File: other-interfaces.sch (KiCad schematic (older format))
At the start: 14 parts, among them J9 693072010801

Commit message: Change uSD card holder
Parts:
- removed J9: 693072010801, sa800u-baseboard-hw-footprints:MicroSD_693072010801, symbol sa800u-baseboard-hw:693072010801
- added J5: DM3AT-SF-PEJM5, antmicro-footprints:MicroSD_DM3AT-SF-PEJM5, symbol antmicroMemoryConnectorsPCCardSockets:DM3AT-SF-PEJM5
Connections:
- wire segments 51 -> 56
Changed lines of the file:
@@
 Text
 Wire Wire Line
-	2700 2600 2700 2675
-Wire Wire Line
-	2700 2275 2700 2300
-Wire Wire Line
-	2500 2275 2700 2275
-Wire Wire Line
-	2700 2675 2675 2675
-Connection ~ 2700 2675
+	5900 3275 5850 3275
+$Comp
+L sa800u-baseboard-hw:GND #PWR?
+U 1 1 61F78331
+P 5850 3775
+AR Path="/61A60486/61F78331" Ref="#PWR?"  Part="1"
+AR Path="/61C01D88/61F78331" Ref="#PWR0191"  Part="1"
+F 0 "#PWR0191" H 5850 3525 50  0001 C CNN
+F 1 "GND" H 5855 3602 50  0000 C CNN
+F 2 "" H 5850 3775 50  0001 C CNN
+F 3 "" H 5850 3775 50  0001 C CNN
+	1    5850 3775
+	1    0    0    -1
+$EndComp
+$Comp
+L sa800u-baseboard-hw:GND #PWR?
+U 1 1 61F9BA66
+P 7650 3725
+AR Path="/61A60486/61F9BA66" Ref="#PWR?"  Part="1"
+AR Path="/61C01D88/61F9BA66" Ref="#PWR0256"  Part="1"
+F 0 "#PWR0256" H 7650 3475 50  0001 C CNN
+F 1 "GND" H 7655 3552 50  0000 C CNN
+F 2 "" H 7650 3725 50  0001 C CNN
+F 3 "" H 7650 3725 50  0001 C CNN
+	1    7650 3725
+	1    0    0    -1
+$EndComp
+Wire Wire Line
+	7600 3675 7650 3675
+Wire Wire Line
+	7650 3675 7650 3725
+Wire Wire Line
+	5850 3675 5850 3775
+$Comp
+L antmicroMemoryConnectorsPCCardSockets:DM3AT-SF-PEJM5 J5
+U 1 1 62685888
+P 6800 3175
+F 0 "J5" H 6750 4174 50  0000 C CNN
+F 1 "DM3AT-SF-PEJM5" H 6750 4083 50  0000 C CNN
+F 2 "antmicro-footprints:MicroSD_DM3AT-SF-PEJM5" H 6800 3175 50  0001 C CNN
+F 3 "" H 6800 3175 50  0001 C CNN
+F 4 "HIROSE" H 6750 3992 50  0000 C CNN "Manufacturer"
+F 5 "DM3AT-SF-PEJM5" H 6750 3901 50  0000 C CNN "MPN"
+	1    6800 3175
+	1    0    0    -1
+$EndComp
+Wire Wire Line
+	5850 3275 5850 3675
+Wire Wire Line
+	5850 3675 5900 3675
+Connection ~ 5850 3675
 Wire Wire Line
 	2725 3475 2675 3475
@@
 	1    0    0    -1
 $EndComp
-Text GLabel 2675 3075 0    50   Input ~ 0
-SD_LDO21A
 $Comp
 L sa800u-baseboard-hw:R_1k_0402 R105
@@
 	1    0    0    -1
 $EndComp
-Text GLabel 2675 2775 0    50   Input ~ 0
-SD_DATA2
-Text GLabel 2675 2875 0    50   Input ~ 0
-SD_DATA3
-Text GLabel 2675 3475 0    50   Input ~ 0
-SD_DATA1
-Text GLabel 2675 3375 0    50   Input ~ 0
-SD_DATA0
-Text GLabel 2675 2675 0    50   Input ~ 0
-SD_DET
-Text GLabel 2675 2975 0    50   Input ~ 0
-SD_CMD
-Text GLabel 2675 3175 0    50   Input ~ 0
-SD_CLK
 Wire Wire Line
 	4250 3725 4250 2775
@@
 Wire Wire Line
 	5375 3725 5375 3475
-Wire Wire Line
-	5900 3275 5850 3275
-$Comp
-L sa800u-baseboard-hw:GND #PWR?
-U 1 1 61F78331
-P 5850 3625
-AR Path="/61A60486/61F78331" Ref="#PWR?"  Part="1"
-AR Path="/61C01D88/61F78331" Ref="#PWR0191"  Part="1"
-F 0 "#PWR0191" H 5850 3375 50  0001 C CNN
-F 1 "GND" H 5855 3452 50  0000 C CNN
-F 2 "" H 5850 3625 50  0001 C CNN
-F 3 "" H 5850 3625 50  0001 C CNN
-	1    5850 3625
-	1    0    0    -1
-$EndComp
 $Comp
 L sa800u-baseboard-hw:GND #PWR?
@@
 Wire Wire Line
 	5075 3725 5075 3075
-$Comp
-L sa800u-baseboard-hw:C_10p_0402 C124
-U 1 1 62000138
-P 5150 2300
-F 0 "C124" H 5265 2345 60  0000 L CNN
-F 1 "C_10p_0402" H 5150 2150 60  0001 C CNN
-F 2 "sa800u-baseboard-hw-footprints:0402-cap" H 5350 2500 60  0001 L CNN
-F 3 "" H 5150 2300 50  0001 C CNN
-F 4 "MULTICOMP" H 5350 2700 60  0001 L CNN "Manufacturer"
-F 5 "MC0402N100D500CT" H 5350 2600 60  0001 L CNN "MPN"
-F 6 "10p" H 5265 2247 50  0000 L CNN "Val"
-	1    5150 2300
-	1    0    0    -1
-$EndComp
-Wire Wire Line
-	5075 2150 5150 2150
-$Comp
-L sa800u-baseboard-hw:GND #PWR?
-U 1 1 62009F3E
-P 5150 2450
-AR Path="/61A60486/62009F3E" Ref="#PWR?"  Part="1"
-AR Path="/61C01D88/62009F3E" Ref="#PWR0184"  Part="1"
-F 0 "#PWR0184" H 5150 2200 50  0001 C CNN
-F 1 "GND" H 5155 2277 50  0000 C CNN
-F 2 "" H 5150 2450 50  0001 C CNN
-F 3 "" H 5150 2450 50  0001 C CNN
-	1    5150 2450
-	1    0    0    -1
-$EndComp
-$Comp
-L sa800u-baseboard-hw:GND #PWR?
-U 1 1 6200C035
-P 5575 2450
-AR Path="/61A60486/6200C035" Ref="#PWR?"  Part="1"
-AR Path="/61C01D88/6200C035" Ref="#PWR0185"  Part="1"
-F 0 "#PWR0185" H 5575 2200 50  0001 C CNN
-F 1 "GND" H 5580 2277 50  0000 C CNN
-F 2 "" H 5575 2450 50  0001 C CNN
-F 3 "" H 5575 2450 50  0001 C CNN
-	1    5575 2450
-	1    0    0    -1
-$EndComp
-Connection ~ 5150 2150
-Wire Wire Line
-	5150 2150 5575 2150
-$Comp
-L sa800u-baseboard-hw:C_2u2_0603 C125
-U 1 1 62000EB0
-P 5575 2300
-F 0 "C125" H 5690 2345 60  0000 L CNN
-F 1 "C_2u2_0603" H 5575 2150 60  0001 C CNN
-F 2 "sa800u-baseboard-hw-footprints:0603-cap" H 5775 2500 60  0001 L CNN
-F 3 "" H 5575 2300 50  0001 C CNN
-F 4 "TDK" H 5775 2700 60  0001 L CNN "Manufacturer"
-F 5 "C1608X5R1V225K080AC" H 5775 2600 60  0001 L CNN "MPN"
-F 6 "2u2" H 5690 2247 50  0000 L CNN "Val"
-	1    5575 2300
-	1    0    0    -1
-$EndComp
 Text Label 3475 2675 0    50   ~ 0
 SD_DET_R
@@
 Wire Wire Line
 	5075 3075 5900 3075
-Text Label 5075 2150 2    50   ~ 0
-SD_VDD_R
 $Comp
 L sa800u-baseboard-hw:R_100k_0402 R104
@@
 	0    1    1    0
 $EndComp
+Wire Wire Line
+	3025 3075 5075 3075
+Connection ~ 5075 3075
+Wire Wire Line
+	3025 3175 5175 3175
+Connection ~ 5175 3175
+Wire Wire Line
+	3025 3375 5275 3375
+Connection ~ 5275 3375
+Wire Wire Line
+	5275 3375 5900 3375
+Wire Wire Line
+	3025 3475 5375 3475
+Connection ~ 5375 3475
+Wire Wire Line
+	5375 3475 5900 3475
+Wire Wire Line
+	3025 2975 4450 2975
+Connection ~ 4450 2975
+Wire Wire Line
+	4450 2975 5900 2975
+Wire Wire Line
+	3025 2875 4350 2875
+Connection ~ 4350 2875
+Wire Wire Line
+	4350 2875 5900 2875
+Wire Wire Line
+	3025 2775 4250 2775
+Connection ~ 4250 2775
+Wire Wire Line
+	4250 2775 5900 2775
+Wire Wire Line
+	3025 2675 4150 2675
+Connection ~ 2700 2675
 Text GLabel 2500 2275 0    50   Input ~ 0
 VREG_S4A_1V8
-Wire Wire Line
-	3025 3075 5075 3075
-Connection ~ 5075 3075
-Wire Wire Line
-	3025 3175 5175 3175
-Connection ~ 5175 3175
-Wire Wire Line
-	3025 3375 5275 3375
-Connection ~ 5275 3375
-Wire Wire Line
-	5275 3375 5900 3375
-Wire Wire Line
-	3025 3475 5375 3475
-Connection ~ 5375 3475
-Wire Wire Line
-	5375 3475 5900 3475
-Wire Wire Line
-	3025 2975 4450 2975
-Connection ~ 4450 2975
-Wire Wire Line
-	4450 2975 5900 2975
-Wire Wire Line
-	3025 2875 4350 2875
-Connection ~ 4350 2875
-Wire Wire Line
-	4350 2875 5900 2875
-Wire Wire Line
-	3025 2775 4250 2775
-Connection ~ 4250 2775
-Wire Wire Line
-	4250 2775 5900 2775
-Wire Wire Line
-	3025 2675 4150 2675
-$Comp
-L sa800u-baseboard-hw:693072010801 J9
-U 1 1 61F945C0
-P 6400 3225
-F 0 "J9" H 6367 3940 50  0000 C CNN
-F 1 "693072010801" H 6367 3849 50  0000 C CNN
-F 2 "sa800u-baseboard-hw-footprints:MicroSD_693072010801" H 6300 2575 50  0001 C CNN
-F 3 "https://www.we-online.com/catalog/datasheet/693072010801.pdf" H 6050 3225 50  0001 C CNN
-F 4 "693072010801" H 6400 3875 50  0001 C CNN "MPN"
-F 5 "Wurth Electronics" H 6350 3975 50  0001 C CNN "Manufacturer"
-	1    6400 3225
-	1    0    0    -1
-$EndComp
-$Comp
-L sa800u-baseboard-hw:GND #PWR?
-U 1 1 61F9BA66
-P 6800 3625
-AR Path="/61A60486/61F9BA66" Ref="#PWR?"  Part="1"
-AR Path="/61C01D88/61F9BA66" Ref="#PWR0256"  Part="1"
-F 0 "#PWR0256" H 6800 3375 50  0001 C CNN
-F 1 "GND" H 6805 3452 50  0000 C CNN
-F 2 "" H 6800 3625 50  0001 C CNN
-F 3 "" H 6800 3625 50  0001 C CNN
-	1    6800 3625
-	1    0    0    -1
-$EndComp
-Wire Wire Line
-	6750 3575 6800 3575
-Wire Wire Line
-	6800 3575 6800 3625
-Wire Wire Line
-	5850 3275 5850 3625
+Text GLabel 2675 3175 0    50   Input ~ 0
+SD_CLK
+Text GLabel 2675 2975 0    50   Input ~ 0
+SD_CMD
+Text GLabel 2675 2675 0    50   Input ~ 0
+SD_DET
+Text GLabel 2675 3375 0    50   Input ~ 0
+SD_DATA0
+Text GLabel 2675 3475 0    50   Input ~ 0
+SD_DATA1
+Text GLabel 2675 2875 0    50   Input ~ 0
+SD_DATA3
+Text GLabel 2675 2775 0    50   Input ~ 0
+SD_DATA2
+Text GLabel 2675 3075 0    50   Input ~ 0
+SD_LDO21A
+Wire Wire Line
+	2700 2675 2675 2675
+Wire Wire Line
+	2500 2275 2700 2275
+Wire Wire Line
+	2700 2275 2700 2300
+Wire Wire Line
+	2700 2600 2700 2675
+Text Label 5075 2150 2    50   ~ 0
+SD_VDD_R
+$Comp
+L sa800u-baseboard-hw:C_2u2_0603 C125
+U 1 1 62000EB0
+P 5575 2300
+F 0 "C125" H 5690 2345 60  0000 L CNN
+F 1 "C_2u2_0603" H 5575 2150 60  0001 C CNN
+F 2 "sa800u-baseboard-hw-footprints:0603-cap" H 5775 2500 60  0001 L CNN
+F 3 "" H 5575 2300 50  0001 C CNN
+F 4 "TDK" H 5775 2700 60  0001 L CNN "Manufacturer"
+F 5 "C1608X5R1V225K080AC" H 5775 2600 60  0001 L CNN "MPN"
+F 6 "2u2" H 5690 2247 50  0000 L CNN "Val"
+	1    5575 2300
+	1    0    0    -1
+$EndComp
+Wire Wire Line
+	5150 2150 5575 2150
+Connection ~ 5150 2150
+$Comp
+L sa800u-baseboard-hw:GND #PWR?
+U 1 1 6200C035
+P 5575 2450
+AR Path="/61A60486/6200C035" Ref="#PWR?"  Part="1"
+AR Path="/61C01D88/6200C035" Ref="#PWR0185"  Part="1"
+F 0 "#PWR0185" H 5575 2200 50  0001 C CNN
+F 1 "GND" H 5580 2277 50  0000 C CNN
+F 2 "" H 5575 2450 50  0001 C CNN
+F 3 "" H 5575 2450 50  0001 C CNN
+	1    5575 2450
+	1    0    0    -1
+$EndComp
+$Comp
+L sa800u-baseboard-hw:GND #PWR?
+U 1 1 62009F3E
+P 5150 2450
+AR Path="/61A60486/62009F3E" Ref="#PWR?"  Part="1"
+AR Path="/61C01D88/62009F3E" Ref="#PWR0184"  Part="1"
+F 0 "#PWR0184" H 5150 2200 50  0001 C CNN
+F 1 "GND" H 5155 2277 50  0000 C CNN
+F 2 "" H 5150 2450 50  0001 C CNN
+F 3 "" H 5150 2450 50  0001 C CNN
+	1    5150 2450
+	1    0    0    -1
+$EndComp
+Wire Wire Line
+	5075 2150 5150 2150
+$Comp
+L sa800u-baseboard-hw:C_10p_0402 C124
+U 1 1 62000138
+P 5150 2300
+F 0 "C124" H 5265 2345 60  0000 L CNN
+F 1 "C_10p_0402" H 5150 2150 60  0001 C CNN
+F 2 "sa800u-baseboard-hw-footprints:0402-cap" H 5350 2500 60  0001 L CNN
+F 3 "" H 5150 2300 50  0001 C CNN
+F 4 "MULTICOMP" H 5350 2700 60  0001 L CNN "Manufacturer"
+F 5 "MC0402N100D500CT" H 5350 2600 60  0001 L CNN "MPN"
+F 6 "10p" H 5265 2247 50  0000 L CNN "Val"
+	1    5150 2300
+	1    0    0    -1
+$EndComp
+Wire Wire Line
+	4150 2675 5725 2675
+Wire Wire Line
+	5725 2675 5725 3575
+Wire Wire Line
+	5725 3575 5900 3575
+Connection ~ 4150 2675
 $EndSCHEMATC

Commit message: Loclib
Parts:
- J5: footprint antmicro-footprints:MicroSD_DM3AT-SF-PEJM5 -> sa800u-baseboard-hw-footprints:MicroSD_DM3AT-SF-PEJM5; symbol antmicroMemoryConnectorsPCCardSockets:DM3AT-SF-PEJM5 -> sa800u-baseboard-hw:DM3AT-SF-PEJM5
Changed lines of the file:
@@
 	5850 3675 5850 3775
 $Comp
-L antmicroMemoryConnectorsPCCardSockets:DM3AT-SF-PEJM5 J5
+L sa800u-baseboard-hw:DM3AT-SF-PEJM5 J5
 U 1 1 62685888
 P 6800 3175
 F 0 "J5" H 6750 4174 50  0000 C CNN
 F 1 "DM3AT-SF-PEJM5" H 6750 4083 50  0000 C CNN
-F 2 "antmicro-footprints:MicroSD_DM3AT-SF-PEJM5" H 6800 3175 50  0001 C CNN
+F 2 "sa800u-baseboard-hw-footprints:MicroSD_DM3AT-SF-PEJM5" H 6800 3175 50  0001 C CNN
 F 3 "" H 6800 3175 50  0001 C CNN
 F 4 "HIROSE" H 6750 3992 50  0000 C CNN "Manufacturer"

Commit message: Add QWIIC connector and connect it to SoM
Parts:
- added C153, C71: C_100n_0402, sa800u-baseboard-hw-footprints:0402-cap, symbol sa800u-baseboard-hw:C_100n_0402
- added J7: BM04B-SRSS-TB-LF-SN, antmicro-footprints:BM04B-SRSS-TB-LF-SN, symbol antmicroRectangularConnectorsHeadersMalePins:BM04B-SRSS-TB-LF-SN
- added R165, R166: R_2k_0402, sa800u-baseboard-hw-footprints:0402-res, symbol sa800u-baseboard-hw:R_2k_0402
- added TP79, TP80, TP81, TP82: TP_SMD_0_75MM, sa800u-baseboard-hw-footprints:Testpoint_smd_0_75mm, symbol sa800u-baseboard-hw:TP_SMD_0_75MM
- added U23: NTS0102GT, sa800u-baseboard-hw-footprints:PSON50P100X195X50-8N, symbol sa800u-baseboard-hw:NTS0102GT
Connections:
- net labels added: 3V3_SYS, I2C10_SCL, I2C10_SCL_3V3, I2C10_SDA, I2C10_SDA_3V3
- wire segments 56 -> 93
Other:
- note added: "Note:\nPullups on SoM.sch"

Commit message: Loclib
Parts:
- J7: footprint antmicro-footprints:BM04B-SRSS-TB-LF-SN -> sa800u-baseboard-hw-footprints:BM04B-SRSS-TB-LF-SN; symbol antmicroRectangularConnectorsHeadersMalePins:BM04B-SRSS-TB-LF-SN -> sa800u-baseboard-hw:BM04B-SRSS-TB-LF-SN
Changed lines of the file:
@@
 Connection ~ 4150 2675
 $Comp
-L antmicroRectangularConnectorsHeadersMalePins:BM04B-SRSS-TB-LF-SN J7
+L sa800u-baseboard-hw:BM04B-SRSS-TB-LF-SN J7
 U 1 1 637F6555
 P 6525 7000
 F 0 "J7" H 6443 6725 50  0000 C CNN
 F 1 "BM04B-SRSS-TB-LF-SN" H 6443 6816 50  0000 C CNN
-F 2 "antmicro-footprints:BM04B-SRSS-TB-LF-SN" H 6525 6750 50  0001 C CNN
+F 2 "sa800u-baseboard-hw-footprints:BM04B-SRSS-TB-LF-SN" H 6525 6750 50  0001 C CNN
 F 3 "https://www.jst-mfg.com/product/pdf/eng/eSH.pdf" H 6075 6700 50  0001 C CNN
 F 4 "BM04B-SRSS-TB(LF)(SN) " H 6425 6650 50  0001 L CNN "MPN"

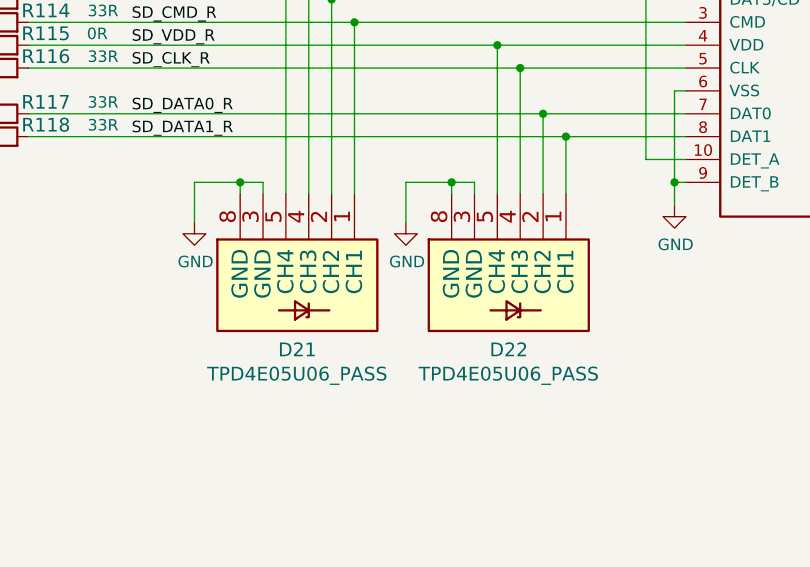
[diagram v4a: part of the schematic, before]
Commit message: Change TSVs to consolidate bom
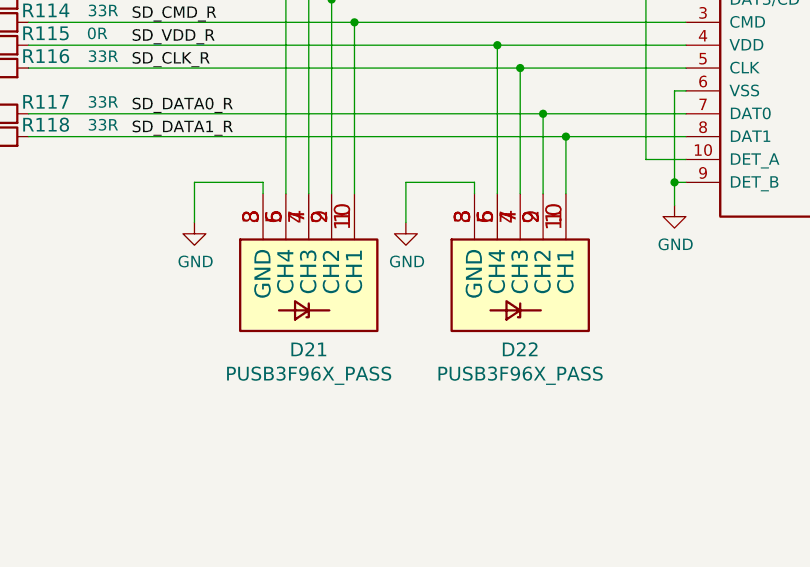
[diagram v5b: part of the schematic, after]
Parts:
- removed D21, D22: TPD4E05U06_PASS, sa800u-baseboard-hw-footprints:TPD4E05U06_PASS, symbol sa800u-baseboard-hw:TPD4E05U06_PASS
- added D21, D22: PUSB3F96X_PASS, sa800u-baseboard-hw-footprints:PUSB3F96X, symbol sa800u-baseboard-hw:PUSB3F96X_PASS
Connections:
- net GND: now also D21.3 (GND), D21.8 (GND), D22.3 (GND), D22.8 (GND)
- net SD_CLK_R: now also D22.4 (CH3), D22.7 (CH3)
- net SD_CMD_R: now also D21.1 (CH1), D21.10 (CH1)
- net SD_DATA0_R: now also D22.2 (CH2), D22.9 (CH2)
- net SD_DATA1_R: now also D22.1 (CH1), D22.10 (CH1)
- net SD_DATA2_R: now also D21.4 (CH3), D21.7 (CH3)
- net SD_DATA3_R: now also D21.2 (CH2), D21.9 (CH2)
- net SD_DET_R: now also D21.5 (CH4), D21.6 (CH4)
- net SD_VDD_R: now also D22.5 (CH4), D22.6 (CH4)
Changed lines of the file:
@@
 $EndComp
-Wire Wire Line
-	3950 3675 3750 3675
-Connection ~ 3950 3675
-Wire Wire Line
-	3950 3725 3950 3675
 Wire Wire Line
 	3750 3675 3750 3850
 Wire Wire Line
-	4050 3675 3950 3675
-Wire Wire Line
 	4050 3725 4050 3675
 Wire Wire Line
-	4875 3675 4675 3675
-Connection ~ 4875 3675
-Wire Wire Line
-	4875 3725 4875 3675
-Wire Wire Line
 	4675 3675 4675 3850
 Wire Wire Line
-	4975 3675 4875 3675
-Wire Wire Line
 	4975 3725 4975 3675
-$Comp
-L sa800u-baseboard-hw:TPD4E05U06_PASS D22
-U 1 1 61F22664
-P 5175 3925
-F 0 "D22" V 5658 3875 60  0000 C CNN
-F 1 "TPD4E05U06_PASS" V 5764 3875 60  0000 C CNN
-F 2 "sa800u-baseboard-hw-footprints:TPD4E05U06_PASS" H 5175 3925 60  0001 C CNN
-F 3 "" H 5175 3925 60  0001 C CNN
-F 4 "Texas Instruments" H 5175 3925 50  0001 C CNN "Manufacturer"
-F 5 "TPD4E05U06DQAR" H 5175 3925 50  0001 C CNN "MPN"
-	1    5175 3925
-	0    1    1    0
-$EndComp
-$Comp
-L sa800u-baseboard-hw:TPD4E05U06_PASS D21
-U 1 1 61F2105E
-P 4250 3925
-F 0 "D21" V 4733 3875 60  0000 C CNN
-F 1 "TPD4E05U06_PASS" V 4839 3875 60  0000 C CNN
-F 2 "sa800u-baseboard-hw-footprints:TPD4E05U06_PASS" H 4250 3925 60  0001 C CNN
-F 3 "" H 4250 3925 60  0001 C CNN
-F 4 "Texas Instruments" H 4250 3925 50  0001 C CNN "Manufacturer"
-F 5 "TPD4E05U06DQAR" H 4250 3925 50  0001 C CNN "MPN"
-	1    4250 3925
-	0    1    1    0
-$EndComp
 Wire Wire Line
 	4150 2675 4150 3725
@@
 Wire Wire Line
 	5725 7050 6325 7050
+$Comp
+L sa800u-baseboard-hw:PUSB3F96X_PASS D?
+U 1 1 62106A90
+P 4250 3925
+AR Path="/6197686D/62106A90" Ref="D?"  Part="1"
+AR Path="/61A2F307/62106A90" Ref="D?"  Part="1"
+AR Path="/61C01D88/62106A90" Ref="D21"  Part="1"
+F 0 "D21" V 4733 3925 60  0000 C CNN
+F 1 "PUSB3F96X_PASS" V 4839 3925 60  0000 C CNN
+F 2 "sa800u-baseboard-hw-footprints:PUSB3F96X" H 4450 3375 60  0001 C CNN
+F 3 "https://pl.mouser.com/datasheet/2/916/PUSB3F96-1600324.pdf" H 4250 3925 60  0001 C CNN
+F 4 "Nexperia" H 4450 3275 50  0001 C CNN "Manufacturer"
+F 5 "PUSB3F96X" H 4450 3275 50  0001 C CNN "MPN"
+	1    4250 3925
+	0    1    1    0
+$EndComp
+Wire Wire Line
+	3750 3675 4050 3675
+$Comp
+L sa800u-baseboard-hw:PUSB3F96X_PASS D?
+U 1 1 6210EEFA
+P 5175 3925
+AR Path="/6197686D/6210EEFA" Ref="D?"  Part="1"
+AR Path="/61A2F307/6210EEFA" Ref="D?"  Part="1"
+AR Path="/61C01D88/6210EEFA" Ref="D22"  Part="1"
+F 0 "D22" V 5658 3925 60  0000 C CNN
+F 1 "PUSB3F96X_PASS" V 5764 3925 60  0000 C CNN
+F 2 "sa800u-baseboard-hw-footprints:PUSB3F96X" H 5375 3375 60  0001 C CNN
+F 3 "https://pl.mouser.com/datasheet/2/916/PUSB3F96-1600324.pdf" H 5175 3925 60  0001 C CNN
+F 4 "Nexperia" H 5375 3275 50  0001 C CNN "Manufacturer"
+F 5 "PUSB3F96X" H 5375 3275 50  0001 C CNN "MPN"
+	1    5175 3925
+	0    1    1    0
+$EndComp
+Wire Wire Line
+	4675 3675 4975 3675
 $EndSCHEMATC

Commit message: Cleanup
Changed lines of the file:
@@
 $Descr A4 11693 8268
 encoding utf-8
-Sheet 9 13
+Sheet 9 12
 Title ""
 Date ""
@@
 Wire Wire Line
 	2700 2600 2700 2675
-Text Label 5075 2150 2    50   ~ 0
+Text Label 4700 2150 0    50   ~ 0
 SD_VDD_R
 $Comp
@@
 $EndComp
 Wire Wire Line
-	5075 2150 5150 2150
+	4700 2150 5150 2150
 $Comp
 L sa800u-baseboard-hw:C_10p_0402 C124
